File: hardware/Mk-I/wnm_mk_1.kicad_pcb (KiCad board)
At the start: 2 copper layers, 96.5 x 66 mm, 121 parts, among them CON1 USB-MICRO-B, SW1 SW_PUSH, SW10 SW_PUSH, SW11 SW_PUSH, SW12 SW_PUSH, SW13 SW_PUSH, SW14 SW_PUSH, SW15 SW_PUSH, SW16 SW_PUSH, SW18 SW_PUSH, SW19 SW_PUSH, SW2 SW_PUSH, SW20 SW_PUSH, SW21 SW_PUSH, SW22 SW_PUSH, SW3 SW_PUSH, SW4 SW_PUSH, SW5 SW_PUSH, SW6 SW_PUSH, SW7 SW_PUSH, SW8 SW_PUSH, SW9 SW_PUSH, U10 STM32_SWD_Connector, U2 MCP73831, U3 BD33IA5, U4 STM32F407VG, U5 SGTL5000, U6 encoder_and_switch, U7 encoder_and_switch, U8 MOLEX_microSD_47219-2001, U9 SSD1306, X1 CRYSTAL

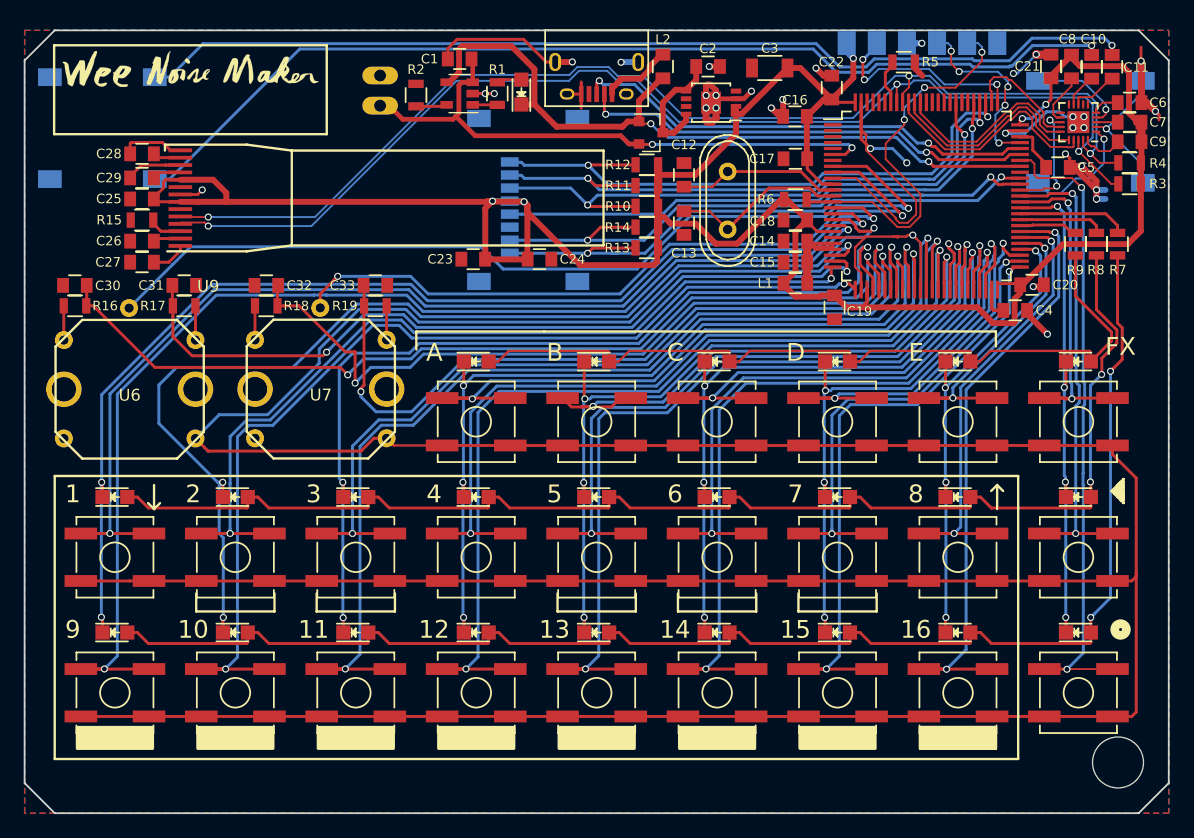
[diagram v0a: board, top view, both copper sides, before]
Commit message: HW: Change most of signal traces to 0.16mm
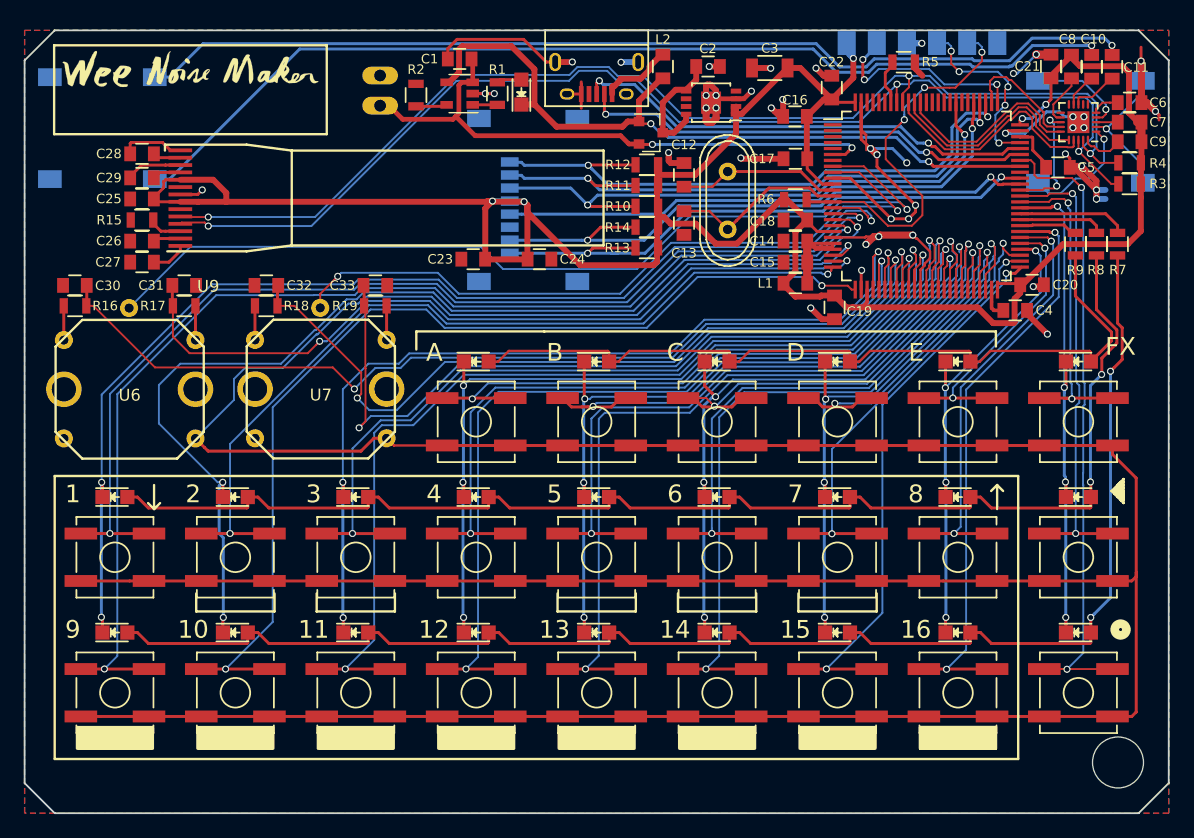
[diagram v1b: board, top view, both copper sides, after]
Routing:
- net GND: track 117.8 -> 125.6 mm, vias 34 -> 45
- net B15: track 52.2 -> 48.9 mm
- net B7: track 41.8 -> 38.5 mm
- net ENC_2_B: track 64.5 -> 67.2 mm
- net COL2: track 95.7 -> 93.2 mm
- net COL3: track 78.6 -> 76.7 mm
- net B6: track 53.3 -> 51.5 mm
- net B14: track 63.6 -> 61.8 mm
- net ENC_2_A: track 67.7 -> 68.9 mm
- net BD: track 33.2 -> 32.0 mm
- net COL7: track 50.6 -> 49.4 mm
- net B13: track 71.8 -> 70.8 mm
- net BB: track 46.8 -> 45.8 mm
- net ENC_1_A: track 78.9 -> 79.9 mm
- net B4: track 70.3 -> 69.6 mm
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
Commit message: HW: Add a DFU mode switch
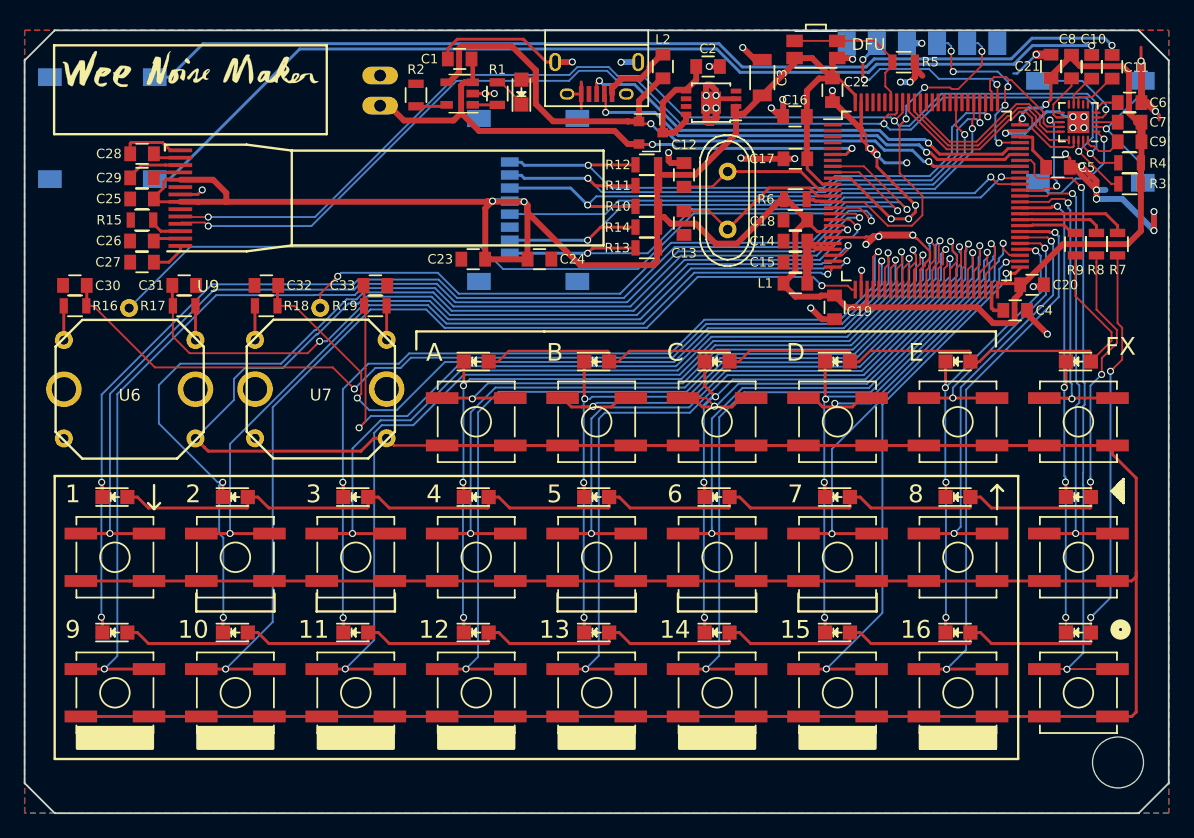
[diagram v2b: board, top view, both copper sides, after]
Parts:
- added DFU_MODE1: Jumper_NO_Small, Buttons_Switches_SMD:SW_SPST_EVQP7A, F.Cu at (146.8, 80.4)
- moved C3 1.03 mm to (142.2, 82.7), turned to 90 degrees
- moved C22 0.24 mm to (148.2, 83.8), turned to 90 degrees
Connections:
- net Net-(R5-Pad1) renamed BOOT0
- BAT1 pad 1: VBUS -> Net-(BAT1-Pad1)
- BAT1 pad 2: Net-(BAT1-Pad2) -> VBUS
- R1 pad 2: Net-(BAT1-Pad2) -> Net-(BAT1-Pad1)
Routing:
- net GND: track 125.6 -> 138.5 mm, vias 45 -> 48
- net BOOT0: track 3.32 -> 12.5 mm
- net 3V3: track 214.2 -> 217.6 mm
- net Net-(BAT1-Pad1): track 0.00 -> 2.89 mm
- net Net-(BAT1-Pad2): track 2.13 -> 0.00 mm
- net NRST: track 33.0 -> 32.1 mm
- net Audio_SCL: track 97.8 -> 97.2 mm
- net SD_DAT1: track 50.4 -> 49.9 mm
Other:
- board text added: "DFU"

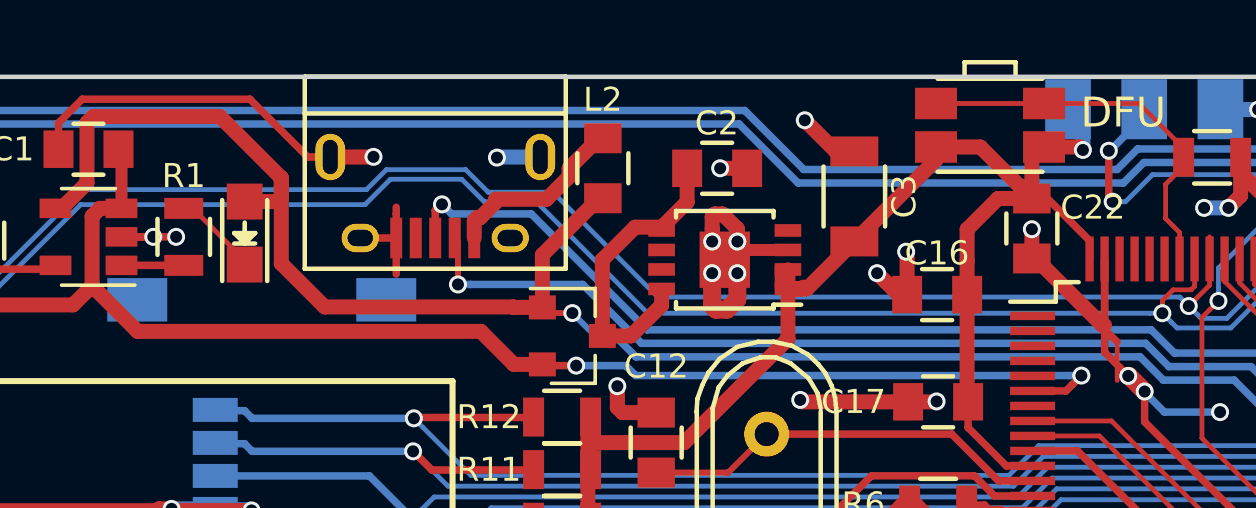
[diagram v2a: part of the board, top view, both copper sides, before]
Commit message: HW: Minor improvement in PCB rounting
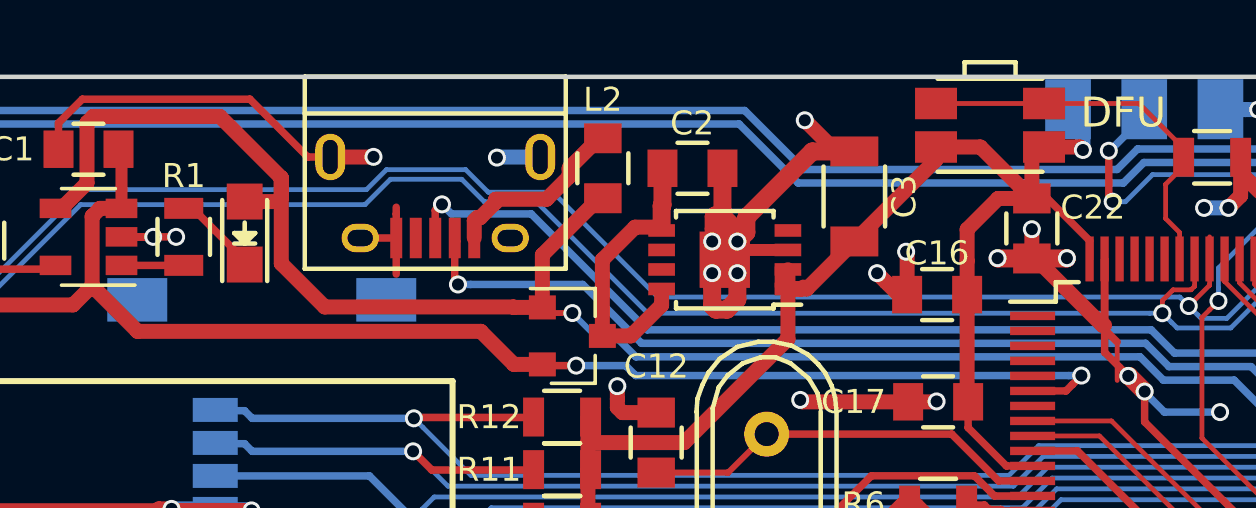
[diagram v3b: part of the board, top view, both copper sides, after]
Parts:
- moved C2 0.82 mm to (136.8, 81.8)
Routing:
- net GND: track 138.5 -> 148.0 mm, vias 48 -> 49
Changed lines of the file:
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@@
   (general
     (links 335)
-    (no_connects 0)
+    (no_connects 1)
     (area 79.934999 78.664999 176.605001 144.855001)
     (thickness 1.6)
     (drawings 96)
-    (tracks 1956)
+    (tracks 1967)
     (zones 0)
     (modules 122)
@@
   )
   (setup
-    (last_trace_width 0.25)
+    (last_trace_width 0.6)
     (user_trace_width 0.16)
     (user_trace_width 0.2)
@@
     (add_net VIN)
   )
+  (module Capacitors_SMD:C_0805 (layer F.Cu)
+    (at 136.8458 81.788)
+    (descr "Capacitor SMD 0805, reflow soldering, AVX (see smccp.pdf)")
+    (tags "capacitor 0805")
+    (attr smd)
+    (fp_text reference C2 (at -0.0127 -1.4986) (layer F.SilkS)
+      (effects (font (size 0.8 0.8) (thickness 0.125)))
+    )
+    (fp_text value 4.7uF (at 0 2.1) (layer F.Fab)
+      (effects (font (size 1 1) (thickness 0.15)))
+    )
+    (fp_line (start -1 0.625) (end -1 -0.625) (layer F.Fab) (width 0.15))
+    (fp_line (start 1 0.625) (end -1 0.625) (layer F.Fab) (width 0.15))
+    (fp_line (start 1 -0.625) (end 1 0.625) (layer F.Fab) (width 0.15))
+    (fp_line (start -1 -0.625) (end 1 -0.625) (layer F.Fab) (width 0.15))
+    (fp_line (start -1.8 -1) (end 1.8 -1) (layer F.CrtYd) (width 0.05))
+    (fp_line (start -1.8 1) (end 1.8 1) (layer F.CrtYd) (width 0.05))
+    (fp_line (start -1.8 -1) (end -1.8 1) (layer F.CrtYd) (width 0.05))
+    (fp_line (start 1.8 -1) (end 1.8 1) (layer F.CrtYd) (width 0.05))
+    (fp_line (start 0.5 -0.85) (end -0.5 -0.85) (layer F.SilkS) (width 0.15))
+    (fp_line (start -0.5 0.85) (end 0.5 0.85) (layer F.SilkS) (width 0.15))
+    (pad 1 smd rect (at -1 0) (size 1 1.25) (layers F.Cu F.Paste F.Mask)
+      (net 42 VIN))
+    (pad 2 smd rect (at 1 0) (size 1 1.25) (layers F.Cu F.Paste F.Mask)
+      (net 31 GND))
+    (model Capacitors_SMD.3dshapes/C_0805.wrl
+      (at (xyz 0 0 0))
+      (scale (xyz 1 1 1))
+      (rotate (xyz 0 0 0))
+    )
+  )
   (module Housings_QFP:LQFP-100_14x14mm_Pitch0.5mm locked (layer F.Cu)
     (at 156.083 92.71)
@@
     )
   )
-  (module Capacitors_SMD:C_0805 (layer F.Cu)
-    (at 137.668 81.788)
-    (descr "Capacitor SMD 0805, reflow soldering, AVX (see smccp.pdf)")
-    (tags "capacitor 0805")
-    (attr smd)
-    (fp_text reference C2 (at -0.0127 -1.4986) (layer F.SilkS)
-      (effects (font (size 0.8 0.8) (thickness 0.125)))
-    )
-    (fp_text value 4.7uF (at 0 2.1) (layer F.Fab)
-      (effects (font (size 1 1) (thickness 0.15)))
-    )
-    (fp_line (start -1 0.625) (end -1 -0.625) (layer F.Fab) (width 0.15))
-    (fp_line (start 1 0.625) (end -1 0.625) (layer F.Fab) (width 0.15))
-    (fp_line (start 1 -0.625) (end 1 0.625) (layer F.Fab) (width 0.15))
-    (fp_line (start -1 -0.625) (end 1 -0.625) (layer F.Fab) (width 0.15))
-    (fp_line (start -1.8 -1) (end 1.8 -1) (layer F.CrtYd) (width 0.05))
-    (fp_line (start -1.8 1) (end 1.8 1) (layer F.CrtYd) (width 0.05))
-    (fp_line (start -1.8 -1) (end -1.8 1) (layer F.CrtYd) (width 0.05))
-    (fp_line (start 1.8 -1) (end 1.8 1) (layer F.CrtYd) (width 0.05))
-    (fp_line (start 0.5 -0.85) (end -0.5 -0.85) (layer F.SilkS) (width 0.15))
-    (fp_line (start -0.5 0.85) (end 0.5 0.85) (layer F.SilkS) (width 0.15))
-    (pad 1 smd rect (at -1 0) (size 1 1.25) (layers F.Cu F.Paste F.Mask)
-      (net 42 VIN))
-    (pad 2 smd rect (at 1 0) (size 1 1.25) (layers F.Cu F.Paste F.Mask)
-      (net 31 GND))
-    (model Capacitors_SMD.3dshapes/C_0805.wrl
-      (at (xyz 0 0 0))
-      (scale (xyz 1 1 1))
-      (rotate (xyz 0 0 0))
-    )
-  )
   (module Capacitors_SMD:C_1206 (layer F.Cu)
     (at 142.24 82.7278 90)
@@
   (via (at 87.20819 121.1834) (size 0.6) (drill 0.4) (layers F.Cu B.Cu) (net 30))
   (segment (start 90.505 121.19) (end 84.755 121.19) (width 0.25) (layer F.Cu) (net 30))
+  (segment (start 148.1582 84.7946) (end 147.0246 84.7946) (width 0.6) (layer F.Cu) (net 31))
+  (segment (start 147.0246 84.7946) (end 147.0152 84.7852) (width 0.6) (layer F.Cu) (net 31))
+  (via (at 147.0152 84.7852) (size 0.6) (drill 0.4) (layers F.Cu B.Cu) (net 31))
+  (segment (start 148.1582 84.7946) (end 149.3172 84.7946) (width 0.6) (layer F.Cu) (net 31))
+  (segment (start 149.3172 84.7946) (end 149.3266 84.7852) (width 0.6) (layer F.Cu) (net 31))
+  (via (at 149.3266 84.7852) (size 0.6) (drill 0.4) (layers F.Cu B.Cu) (net 31))
+  (segment (start 138.342 84.23059) (end 138.641999 83.930591) (width 0.6) (layer F.Cu) (net 31))
+  (segment (start 138.641999 83.930591) (end 138.641999 83.425801) (width 0.6) (layer F.Cu) (net 31))
+  (segment (start 138.641999 83.425801) (end 140.84 81.2278) (width 0.6) (layer F.Cu) (net 31))
+  (segment (start 140.84 81.2278) (end 142.24 81.2278) (width 0.6) (layer F.Cu) (net 31))
+  (segment (start 137.8458 81.788) (end 137.8458 83.73439) (width 0.6) (layer F.Cu) (net 31))
+  (segment (start 137.8458 83.73439) (end 138.342 84.23059) (width 0.6) (layer F.Cu) (net 31))
   (segment (start 154.7114 83.1088) (end 153.898598 83.1088) (width 0.5) (layer B.Cu) (net 31))
   (via (at 153.898598 83.1088) (size 0.6) (drill 0.4) (layers F.Cu B.Cu) (net 31))
@@
   (segment (start 150.583 87.1592) (end 151.003 87.5792) (width 0.25) (layer F.Cu) (net 31))
   (segment (start 138.487 84.511) (end 138.342 84.366) (width 0.4) (layer F.Cu) (net 31))
-  (segment (start 138.668 81.788) (end 137.768002 81.788) (width 0.5) (layer F.Cu) (net 31))
-  (via (at 137.768002 81.788) (size 0.6) (drill 0.4) (layers F.Cu B.Cu) (net 31))
   (via (at 126.2126 81.407) (size 0.6) (drill 0.4) (layers F.Cu B.Cu) (net 31))
   (segment (start 124.7709 81.41254) (end 126.20706 81.41254) (width 0.5) (layer F.Cu) (net 31))
@@
   (segment (start 115.486 85.151) (end 115.613 85.024) (width 0.25) (layer F.Cu) (net 40))
   (segment (start 113.03 85.151) (end 115.486 85.151) (width 0.25) (layer F.Cu) (net 40))
+  (segment (start 135.8458 81.788) (end 135.8458 83.013) (width 0.6) (layer F.Cu) (net 42))
+  (segment (start 135.8458 83.013) (end 135.817 83.0418) (width 0.6) (layer F.Cu) (net 42))
+  (segment (start 135.817 83.0418) (end 135.817 83.700999) (width 0.6) (layer F.Cu) (net 42))
   (segment (start 133.842 87.376) (end 133.842 84.840998) (width 0.5) (layer F.Cu) (net 42))
   (segment (start 133.842 84.840998) (end 134.931999 83.750999) (width 0.5) (layer F.Cu) (net 42))
   (segment (start 134.931999 83.750999) (end 135.830001 83.750999) (width 0.5) (layer F.Cu) (net 42))
-  (segment (start 136.668 81.788) (end 136.668 82.913) (width 0.5) (layer F.Cu) (net 42))
-  (segment (start 136.668 82.913) (end 135.830001 83.750999) (width 0.5) (layer F.Cu) (net 42))
   (segment (start 133.842 87.376) (end 134.792 87.376) (width 0.5) (layer F.Cu) (net 42))
   (segment (start 134.792 87.376) (end 135.817 86.351) (width 0.5) (layer F.Cu) (net 42))
@@
   (segment (start 162.083 84.81) (end 162.083 83.346659) (width 0.16) (layer F.Cu) (net 46))
   (segment (start 162.083 83.346659) (end 162.033741 83.2974) (width 0.16) (layer F.Cu) (net 46))
-  (segment (start 129.028113 85.66079) (end 129.028113 84.219753) (width 0.2) (layer F.Cu) (net 51))
+  (segment (start 129.028113 85.66079) (end 128.9209 85.553577) (width 0.25) (layer F.Cu) (net 51))
+  (segment (start 128.9209 85.553577) (end 128.9209 84.11254) (width 0.25) (layer F.Cu) (net 51))
   (segment (start 129.028113 84.219753) (end 128.9209 84.11254) (width 0.2) (layer F.Cu) (net 51))
   (segment (start 135.148165 87.622811) (end 133.186144 85.66079) (width 0.25) (layer B.Cu) (net 51))
@@
   (segment (start 163.11941 89.21) (end 162.7 89.629411) (width 0.25) (layer F.Cu) (net 51))
   (segment (start 163.983 89.21) (end 163.11941 89.21) (width 0.25) (layer F.Cu) (net 51))
-  (segment (start 128.9209 85.553577) (end 129.028113 85.66079) (width 0.25) (layer F.Cu) (net 51))
   (via (at 129.028113 85.66079) (size 0.6) (drill 0.4) (layers F.Cu B.Cu) (net 51))
   (via (at 156.099305 89.03166) (size 0.6) (drill 0.4) (layers F.Cu B.Cu) (net 51))
@@
   (via (at 160.7693 80.519491) (size 0.6) (drill 0.4) (layers F.Cu B.Cu) (net 127))
   (via (at 155.929017 83.560194) (size 0.6) (drill 0.4) (layers F.Cu B.Cu) (net 127))
-  (segment (start 121.92 84.99602) (end 121.92 84.856) (width 0.16) (layer F.Cu) (net 129))
-  (segment (start 121.92 84.856) (end 120.188 83.124) (width 0.16) (layer F.Cu) (net 129))
-  (segment (start 120.188 83.124) (end 119.888 83.124) (width 0.16) (layer F.Cu) (net 129))
+  (segment (start 121.92 84.99602) (end 121.92 84.856) (width 0.25) (layer F.Cu) (net 129))
+  (segment (start 121.92 84.856) (end 120.188 83.124) (width 0.25) (layer F.Cu) (net 129))
+  (segment (start 120.188 83.124) (end 119.888 83.124) (width 0.25) (layer F.Cu) (net 129))
   (segment (start 148.5646 79.629) (end 151.7246 79.629) (width 0.16) (layer F.Cu) (net 130))
   (segment (start 151.7246 79.629) (end 153.21784 81.12224) (width 0.16) (layer F.Cu) (net 130))

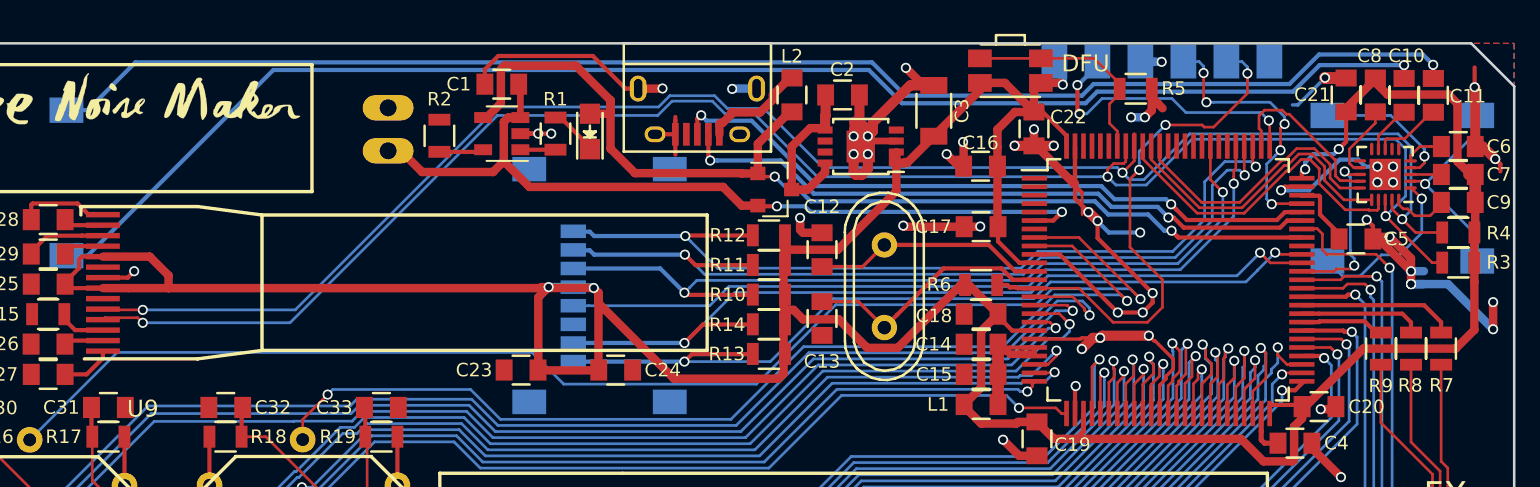
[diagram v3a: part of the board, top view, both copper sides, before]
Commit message: HW: Add screen reset line and some ground path tweaking
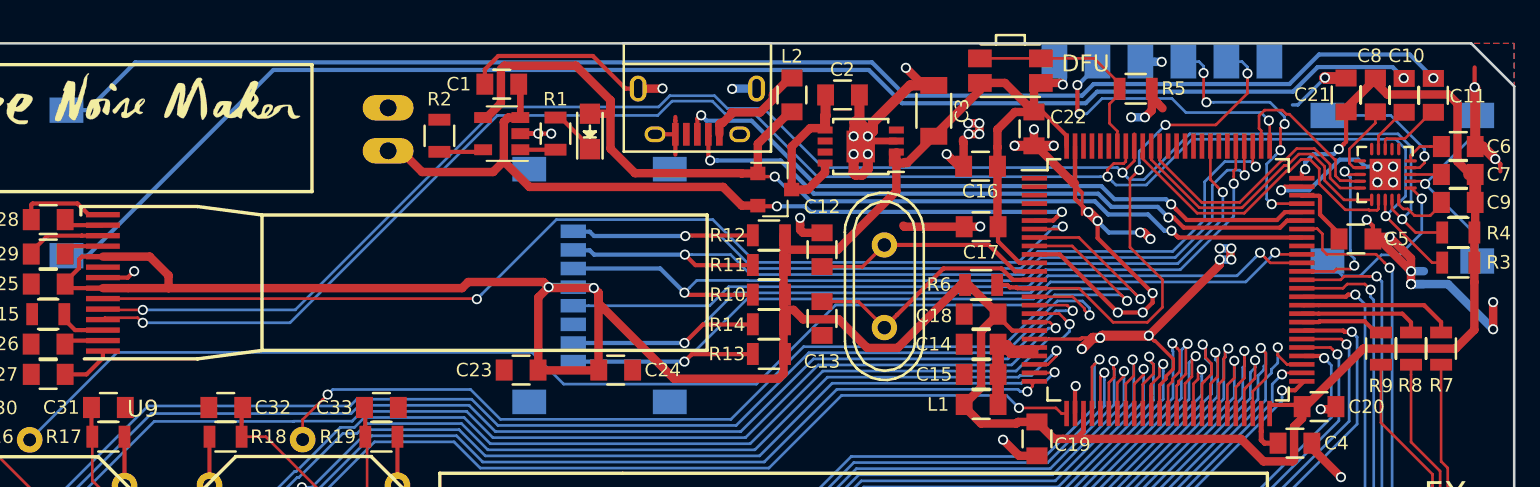
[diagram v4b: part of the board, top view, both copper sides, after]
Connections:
- U4 pad 7: Net-(U4-Pad7) -> Screen_NReset
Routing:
- net Screen_NReset: track 0.00 -> 62.3 mm, vias 0 -> 2
- net GND: track 148.0 -> 159.0 mm, vias 49 -> 56
- net Net-(C14-Pad2): track 10.3 -> 11.6 mm
- net Net-(C10-Pad1): track 86.1 -> 85.6 mm
